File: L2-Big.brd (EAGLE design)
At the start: 10 parts

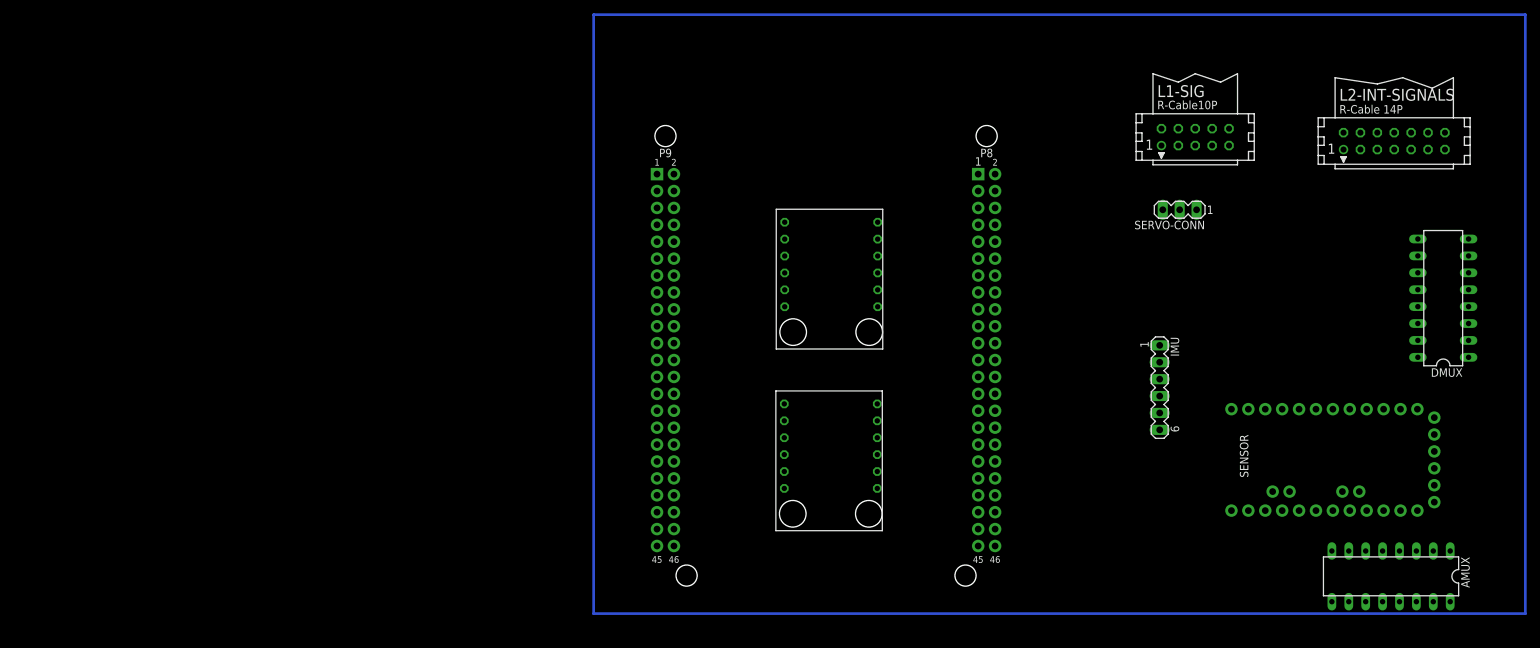
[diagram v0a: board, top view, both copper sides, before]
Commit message: redesigned all boards.
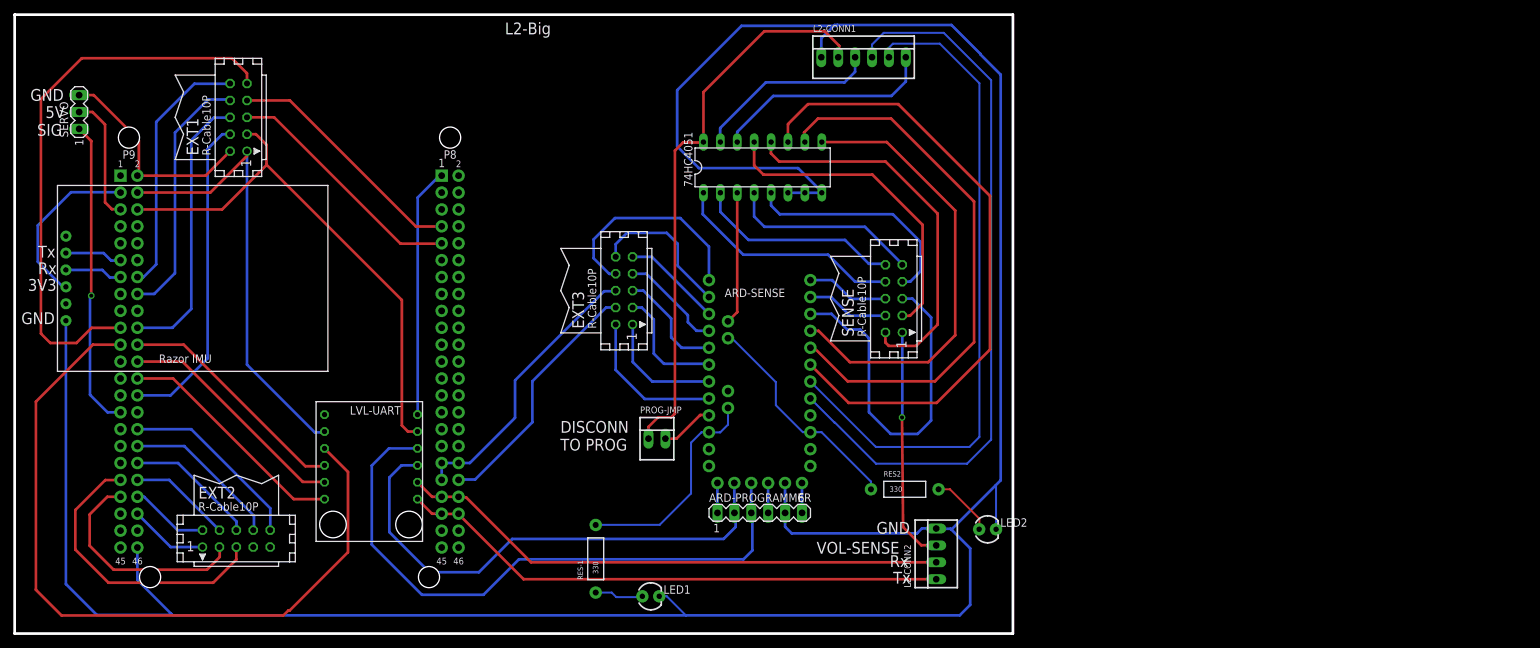
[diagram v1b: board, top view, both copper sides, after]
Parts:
- removed AMUX, DMUX: (no value), 40xx:DIL16
- removed E$8, LVL-SHIFTER1: (no value), levelShifter:LEVEL-SHIFTER
- removed IMU: (no value), con-lstb:MA06-1
- removed L1-SIG: (no value), con-harting:CON10
- removed L2-INT-SIGNALS: (no value), con-harting:CON14
- removed SENSOR: (no value), SparkFun-Boards:ARDUINO_PRO_MINI
- removed SERVO-CONN: (no value), con-lstb:MA03-1
- added 74HC4051: (no value), 40xx:DIL16
- added ARD-PROGRAMMER: (no value), con-lstb:MA06-1
- added ARD-SENSE: (no value), SparkFun-Boards:ARDUINO_PRO_MINI
- added BBB: (no value), SparkFun-Boards:BEAGLE_BONE_BLACK_CAPE
- added EXT1, EXT2, EXT3, SENSE: (no value), con-harting:CON10
- added L2-CONN1: (no value), con-molex:22-23-2061
- added L2-CONN2: (no value), con-molex:22-23-2041
- added LED1, LED2: Blue, SparkFun-LED:LED3MM
- added LVL-UART: (no value), levelShifter:LEVEL-SHIFTER
- added PROG-JMP: (no value), con-molex:22-23-2021
- added RES-1, RES2: 330, SparkFun-Resistors:AXIAL-0.4
- added SERVO: (no value), con-lstb:MA03-1
- E$1: device SparkFun-Boards:BEAGLE_BONE_BLACK_CAPE -> RazorIMU:RAZOR-IMU
- moved E$1 101.4 mm to (-80.6, 36.4), turned to 0 degrees
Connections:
- new net S$1: ARD-SENSE.20, EXT3.2
- new net S$15: 74HC4051.11, ARD-SENSE.7
- new net S$16: ARD-SENSE.11, SENSE.4
- new net S$17: ARD-SENSE.12, SENSE.6
- new net S$18: ARD-SENSE.10, SENSE.5
- new net S$19: 74HC4051.13, SENSE.3
- new net S$20: 74HC4051.12, SENSE.2
- new net S$21: BBB.P9.19, EXT1.9
- new net S$22: ARD-SENSE.16, EXT3.7
- new net S$23: ARD-SENSE.15, EXT3.9
- new net S$24: ARD-SENSE.14, EXT3.10
- new net S$25: ARD-SENSE.13, EXT3.8
- new net S$26: BBB.P9.24, LVL-UART.P$5
- new net S$27: BBB.P9.26, LVL-UART.P$6
- new net S$28: BBB.P8.41, BBB.P8.42, L2-CONN2.1, LVL-UART.P$12
- new net S$29: BBB.P8.39, BBB.P8.40, L2-CONN2.2, LVL-UART.P$11
- new net S$30: BBB.P9.22, LVL-UART.P$4
- new net S$31: BBB.P9.21, LVL-UART.P$3
- new net S$32: 74HC4051.3, ARD-SENSE.A6
- new net S$33: ARD-PROGRAMMER.2, ARD-SENSE.TXO, LVL-UART.P$10
- new net S$34: ARD-PROGRAMMER.3, ARD-SENSE.RXI, LVL-UART.P$9
- new net S$35: BBB.P8.38, EXT3.4
- new net S$36: BBB.P8.35, BBB.P8.36, BBB.P8.37, EXT3.6
- new net S$37: BBB.P8.1, LVL-UART.P$7
- new net S$38: BBB.P9.4, EXT1.1, LVL-UART.P$2
- new net S$39: BBB.P9.6, EXT1.3, LVL-UART.P$8
- new net S$40: BBB.P9.2, EXT1.2, SERVO.3
- new net S$41: BBB.P9.5, SERVO.2
- new net S$42: BBB.P9.14, EXT1.10
- new net S$43: BBB.P9.39, EXT2.3
- new net S$44: BBB.P9.37, EXT2.5
- new net S$45: ARD-SENSE.6, L2-CONN1.5
- new net S$46: ARD-SENSE.5, L2-CONN1.4
- new net S$47: BBB.P9.42, EXT2.1
- new net S$48: BBB.P9.40, EXT2.2
- new net S$49: BBB.P9.38, EXT2.4
- new net S$50: BBB.P9.36, EXT2.6
- new net S$51: BBB.P9.34, EXT2.8
- new net S$52: BBB.P9.32, EXT2.10
- new net S$53: BBB.P9.11, E$1.P$5
- new net S$54: BBB.P9.13, E$1.P$4
- new net S$55: ARD-SENSE.21, PROG-JMP.2
- new net S$56: ARD-SENSE.3, ARD-SENSE.A7, RES2.P$1
- new net S$57: BBB.P9.16, EXT1.8
- new net S$58: BBB.P9.20, EXT1.6
- new net S$59: BBB.P9.28, EXT1.4
- new net S$60: LED2.A, RES2.P$2
- new net S$61: BBB.P8.7, EXT1.7
- new net S$62: BBB.P8.9, EXT1.5
- new net S$63: BBB.P9.29, SERVO.1
- new net S$64: BBB.P9.3, E$1.P$3
- new net S$65: ARD-PROGRAMMER.1, ARD-SENSE.GRN
- new net S$66: ARD-PROGRAMMER.4, ARD-SENSE.VCC
- new net S$67: ARD-PROGRAMMER.6, ARD-SENSE.BLK
- new net S$68: 74HC4051.6, 74HC4051.7, 74HC4051.8, ARD-PROGRAMMER.5, ARD-SENSE.GND, BBB.P9.46, E$1.P$1, L2-CONN1.1, L2-CONN2.4, LED1.K, LED2.K
- new net S$69: ARD-SENSE.22, ARD-SENSE.A5, RES-1.P$2
- new net S$70: LED1.A, RES-1.P$1
- net S$10: now also 74HC4051.1, SENSE.8; no longer AMUX.11, SENSOR.14
- net S$11: now also 74HC4051.4, SENSE.9; no longer AMUX.10, SENSOR.15
- net S$12: now also 74HC4051.5, SENSE.7; no longer AMUX.9, SENSOR.16
- net S$13: now also 74HC4051.9, ARD-SENSE.9; no longer DMUX.5, SENSOR.5
- net S$14: now also 74HC4051.10, ARD-SENSE.8; no longer AMUX.3, SENSOR.A4
- net S$2: now also ARD-SENSE.19, EXT3.1; no longer L2-INT-SIGNALS.7, SENSOR.10
- net S$3: now also ARD-SENSE.18, EXT3.3; no longer L1-SIG.9, SENSOR.9
- net S$4: now also ARD-SENSE.17, EXT3.5; no longer L1-SIG.4, SENSOR.8
- net S$5: now also L2-CONN2.3, SENSE.1; no longer L1-SIG.3, SENSOR.7
- net S$6: now also 74HC4051.15, L2-CONN1.3; no longer L2-INT-SIGNALS.14, SENSOR.6
- net S$7: now also 74HC4051.16, L2-CONN1.2, PROG-JMP.1; no longer DMUX.11, SENSOR.11
- net S$8: now also 74HC4051.14, L2-CONN1.6; no longer DMUX.10, SENSOR.12
- net S$9: now also 74HC4051.2, SENSE.10; no longer DMUX.9, SENSOR.13
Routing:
- net S$1: track 460.0 -> 22.7 mm
- net S$68: track 0.00 -> 418.4 mm
- net S$31: track 0.00 -> 114.0 mm
- net S$46: track 0.00 -> 110.2 mm
- net S$45: track 0.00 -> 101.0 mm
- net S$15: track 0.00 -> 95.8 mm
- net S$34: track 0.00 -> 93.3 mm
- net S$7: track 0.00 -> 85.3 mm
- net S$21: track 0.00 -> 84.7 mm
- net S$14: track 0.00 -> 83.3 mm
- net S$28: track 0.00 -> 83.0 mm
- net S$29: track 0.00 -> 82.9 mm
- net S$39: track 0.00 -> 79.1 mm
- net S$33: track 0.00 -> 77.3 mm
- net S$13: track 0.00 -> 68.4 mm
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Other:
- board outline added: 150 x 93 mm
- board text added: "3V3"
- board text added: "5V"
- board text added: "DISCONN TO PROG"
- board text added: "GND"
- board text added: "L2-Big"
- board text added: "Rx"
- board text added: "SIG"
- board text added: "Tx"
- board text added: "VOL-SENSE"
